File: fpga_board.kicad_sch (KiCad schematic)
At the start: 52 parts, among them J2 FPGA_board, J6 Conn_01x08, SW1 SW_Push, SW10 SW_Push, SW11 SW_DIP_x06, SW12 SW_DIP_x06, SW2 SW_Push, SW3 SW_Push, SW4 SW_Push, SW5 SW_Push, SW6 SW_Push, SW7 SW_Push, SW8 SW_Push, SW9 SW_Push

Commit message: Fix errors with LCD connection
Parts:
- removed R10, R11, R12, R13, R14, R15, R16, R9: 10k, Resistor_SMD:R_1206_3216Metric_Pad1.30x1.75mm_HandSolder, symbol Device:R
- removed R4, R5, R6, R7, R8: 0, Resistor_SMD:R_1206_3216Metric_Pad1.30x1.75mm_HandSolder, symbol Device:R
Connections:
- net GND: now also R1.1, R2.1, R3.1
- net J5: now also J6.3 (Pin_3), SW11.11, SW12.2; no longer J6.4 (Pin_4), SW11.10, SW12.3
- net M2: now also J6.4 (Pin_4), SW11.10, SW12.3; no longer J6.3 (Pin_3), SW11.11, SW12.2
- net N4: no longer R1.1
- net R3: no longer R3.1
- net T2: no longer R2.1
- net LCD/R5 renamed LCD/R0
- net LCD/R6 renamed LCD/G0
- net LCD/R7 renamed LCD/B0

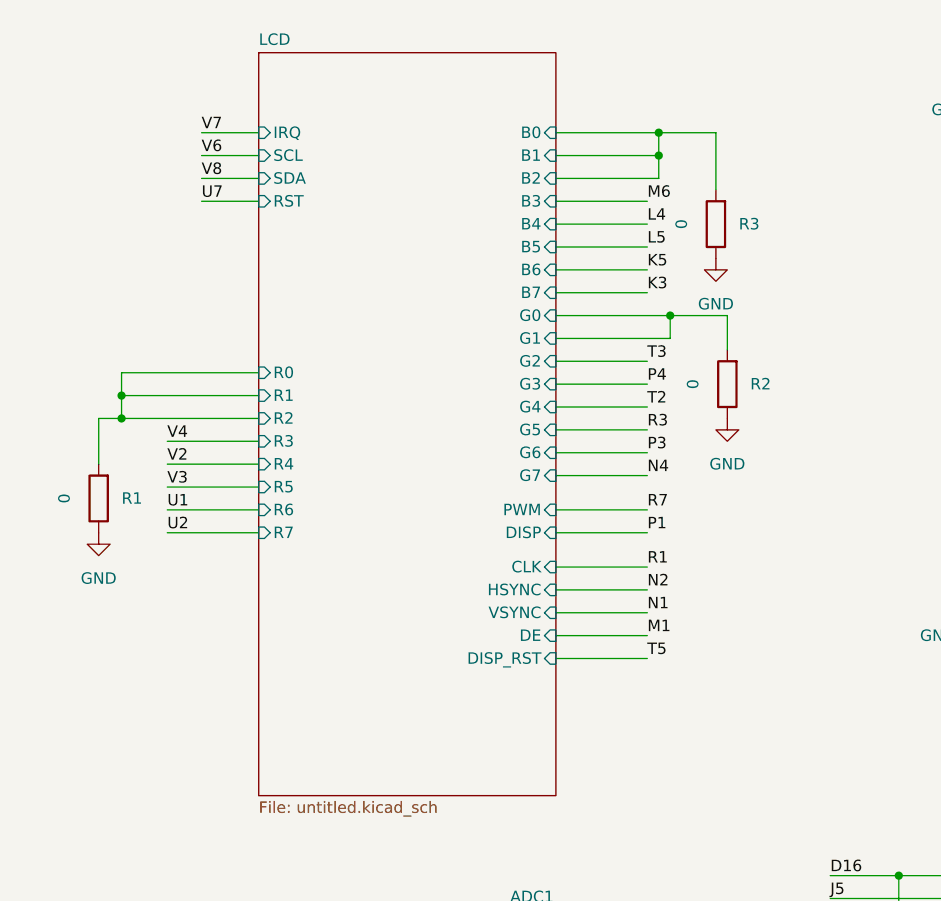
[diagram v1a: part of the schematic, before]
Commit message: edit lcd symbol
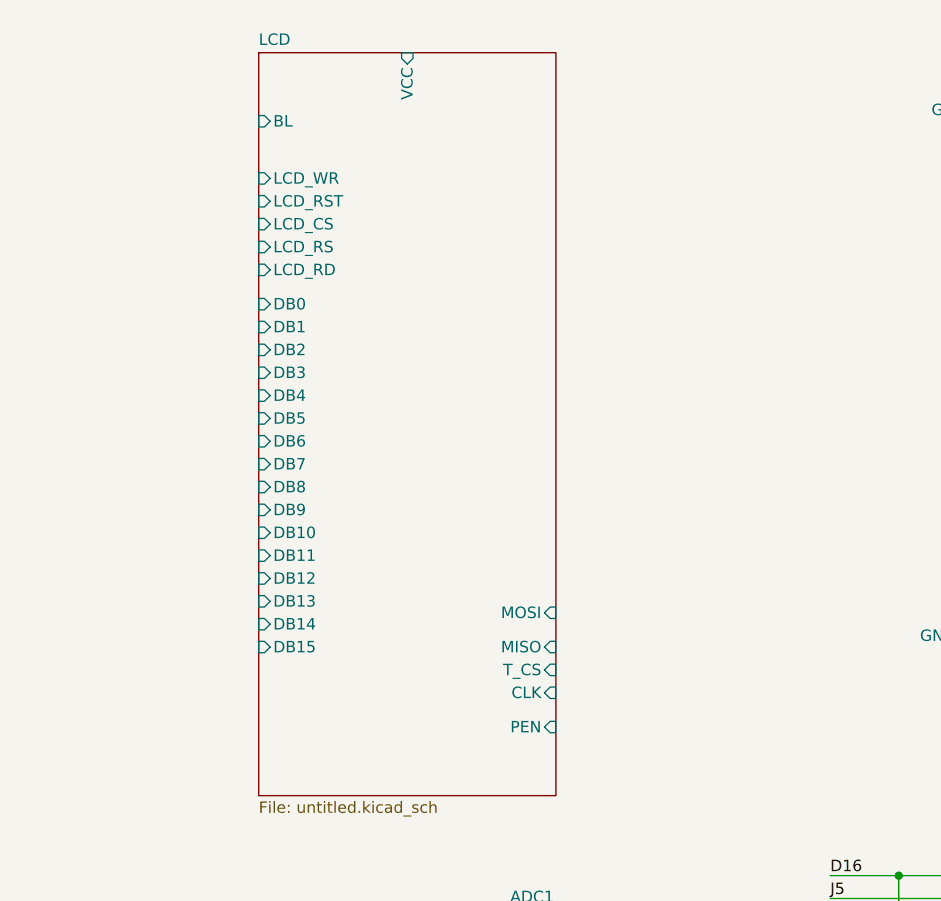
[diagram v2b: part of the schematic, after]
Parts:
- removed R1, R2, R3: 0, Resistor_SMD:R_1206_3216Metric_Pad1.30x1.75mm_HandSolder, symbol Device:R
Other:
- sheet LCD ports: added BL, DB0, DB1, DB10, DB11, DB12, DB13, DB14, DB15, DB2, DB3, DB4, DB5, DB6, DB7, DB8, DB9, LCD_CS, LCD_RD, LCD_RS, LCD_RST, LCD_WR, MISO, MOSI, PEN, T_CS, VCC; removed B0, B1, B2, B3, B4, B5, B6, B7, DE, DISP, DISP_RST, G0, G1, G2, G3, G4, G5, G6, G7, HSYNC, IRQ, PWM, R0, R1, R2, R3, R4, R5, R6, R7, RST, SCL, SDA, VSYNC

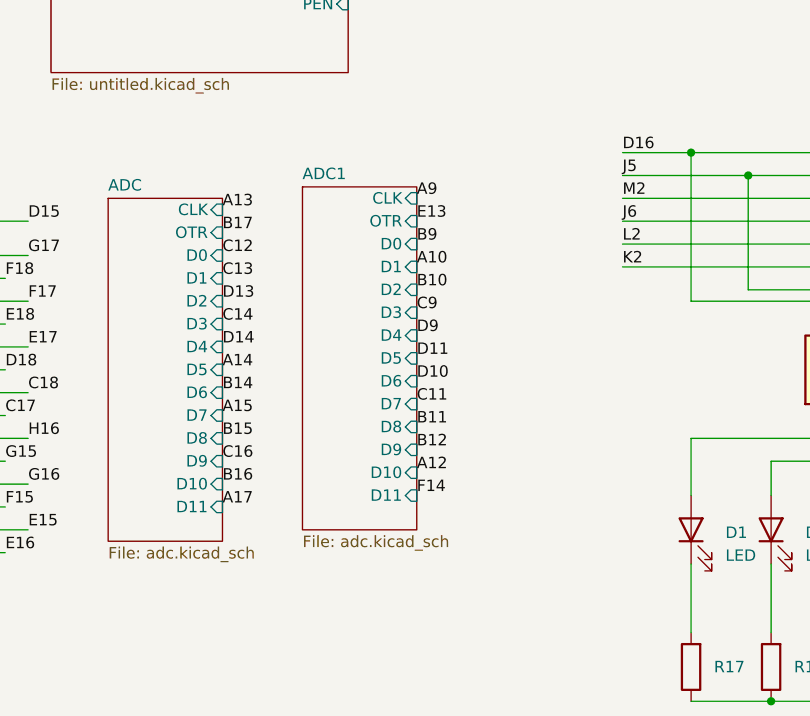
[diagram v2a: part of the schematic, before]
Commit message: Make 3d model for ADC and FPGA. Trying to assembly
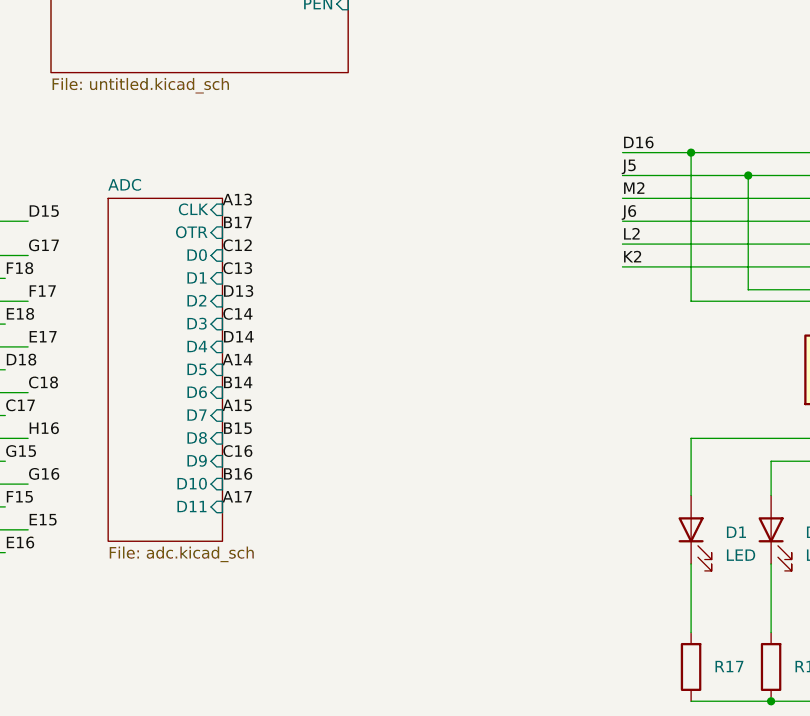
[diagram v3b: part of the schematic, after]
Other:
- removed sheet ADC1
